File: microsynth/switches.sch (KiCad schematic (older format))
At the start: 35 parts, among them SW12 SW_DPTT_SELECTOR, SW13 SW_DPTT_SELECTOR, SW14 SW_SPDT, SW15 SW_SPDT, SW16 SW_SPDT, SW17 SW_SPDT, SW2 SW_Rotary2x6, SW21 SW_Rotary2x6, SW3 SW_DPTT_SELECTOR, SW4 SW_DPTT_SELECTOR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

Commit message: Footprints 2
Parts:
- C8: footprint (none) -> Capacitor_THT:C_Disc_D5.0mm_W2.5mm_P5.00mm
- SW12, SW13, SW3, SW4, SW6: footprint (none) -> Button_Switch_THT:46313LDRX
- SW2, SW21: footprint (none) -> Rotary_Encoder:rotary-12
- U22: footprint (none) -> Package_DIP:DIP-14_W7.62mm_LongPads
- U7: footprint (none) -> Package_DIP:DIP-8_W7.62mm_LongPads
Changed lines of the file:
@@
 F 0 "SW6" H 2394 3979 50  0000 L CNN
 F 1 "SW_DPTT_SELECTOR" H 2394 3888 50  0000 L CNN
-F 2 "" H 2200 3850 50  0001 C CNN
+F 2 "Button_Switch_THT:46313LDRX" H 2200 3850 50  0001 C CNN
 F 3 "" H 2200 3850 50  0001 C CNN
 	2    2200 3850
@@
 F 0 "SW3" H 7594 1338 50  0000 L CNN
 F 1 "SW_DPTT_SELECTOR" H 7594 1247 50  0000 L CNN
-F 2 "" H 7400 1350 50  0001 C CNN
+F 2 "Button_Switch_THT:46313LDRX" H 7400 1350 50  0001 C CNN
 F 3 "" H 7400 1350 50  0001 C CNN
 	1    7400 1350
@@
 F 0 "SW3" H 7594 1379 50  0000 L CNN
 F 1 "SW_DPTT_SELECTOR" H 7594 1288 50  0000 L CNN
-F 2 "" H 7400 1250 50  0001 C CNN
+F 2 "Button_Switch_THT:46313LDRX" H 7400 1250 50  0001 C CNN
 F 3 "" H 7400 1250 50  0001 C CNN
 	2    7400 1250
@@
 F 0 "SW4" H 9344 1338 50  0000 L CNN
 F 1 "SW_DPTT_SELECTOR" H 9344 1247 50  0000 L CNN
-F 2 "" H 9150 1350 50  0001 C CNN
+F 2 "Button_Switch_THT:46313LDRX" H 9150 1350 50  0001 C CNN
 F 3 "" H 9150 1350 50  0001 C CNN
 	1    9150 1350
@@
 F 0 "SW4" H 9344 1379 50  0000 L CNN
 F 1 "SW_DPTT_SELECTOR" H 9344 1288 50  0000 L CNN
-F 2 "" H 9150 1250 50  0001 C CNN
+F 2 "Button_Switch_THT:46313LDRX" H 9150 1250 50  0001 C CNN
 F 3 "" H 9150 1250 50  0001 C CNN
 	2    9150 1250
@@
 F 0 "U22" H 9650 3581 50  0000 C CNN
 F 1 "4013" H 9650 3490 50  0000 C CNN
-F 2 "" H 9650 3100 50  0001 C CNN
+F 2 "Package_DIP:DIP-14_W7.62mm_LongPads" H 9650 3100 50  0001 C CNN
 F 3 "http://www.onsemi.com/pub/Collateral/MC14013B-D.PDF" H 9650 3100 50  0001 C CNN
 	1    9650 3100
@@
 F 0 "U22" H 8980 4396 50  0000 L CNN
 F 1 "4013" H 8980 4305 50  0000 L CNN
-F 2 "" H 8750 4350 50  0001 C CNN
+F 2 "Package_DIP:DIP-14_W7.62mm_LongPads" H 8750 4350 50  0001 C CNN
 F 3 "http://www.onsemi.com/pub/Collateral/MC14013B-D.PDF" H 8750 4350 50  0001 C CNN
 	3    8750 4350
@@
 F 0 "U22" H 9650 4831 50  0000 C CNN
 F 1 "4013" H 9650 4740 50  0000 C CNN
-F 2 "" H 9650 4350 50  0001 C CNN
+F 2 "Package_DIP:DIP-14_W7.62mm_LongPads" H 9650 4350 50  0001 C CNN
 F 3 "http://www.onsemi.com/pub/Collateral/MC14013B-D.PDF" H 9650 4350 50  0001 C CNN
 	2    9650 4350
@@
 F 0 "SW2" H 1750 7221 50  0000 C CNN
 F 1 "SW_Rotary2x6" H 1750 7130 50  0000 C CNN
-F 2 "" H 1600 6950 50  0001 C CNN
+F 2 "Rotary_Encoder:rotary-12" H 1600 6950 50  0001 C CNN
 F 3 "http://cdn-reichelt.de/documents/datenblatt/C200/DS-Serie%23LOR.pdf" H 1600 6950 50  0001 C CNN
 F 4 "Range" H 1750 7039 50  0000 C CNN "Label"
@@
 F 0 "U7" H 3300 7281 50  0000 C CNN
 F 1 "LM741" H 3300 7190 50  0000 C CNN
-F 2 "" H 3350 6850 50  0001 C CNN
+F 2 "Package_DIP:DIP-8_W7.62mm_LongPads" H 3350 6850 50  0001 C CNN
 F 3 "http://www.ti.com/lit/ds/symlink/lm741.pdf" H 3450 6950 50  0001 C CNN
 	1    3300 6800
@@
 F 0 "C8" V 3052 6500 50  0000 C CNN
 F 1 "10n" V 2961 6500 50  0000 C CNN
-F 2 "" H 2838 6350 50  0001 C CNN
+F 2 "Capacitor_THT:C_Disc_D5.0mm_W2.5mm_P5.00mm" H 2838 6350 50  0001 C CNN
 F 3 "~" H 2800 6500 50  0001 C CNN
 	1    2800 6500
@@
 F 0 "SW6" H 2894 2738 50  0000 L CNN
 F 1 "SW_DPTT_SELECTOR" H 2894 2647 50  0000 L CNN
-F 2 "" H 2700 2750 50  0001 C CNN
+F 2 "Button_Switch_THT:46313LDRX" H 2700 2750 50  0001 C CNN
 F 3 "" H 2700 2750 50  0001 C CNN
 	1    2700 2750
@@
 F 0 "SW21" H 1850 2631 50  0000 C CNN
 F 1 "SW_Rotary2x6" H 1850 2540 50  0000 C CNN
-F 2 "" H 1700 2450 50  0001 C CNN
+F 2 "Rotary_Encoder:rotary-12" H 1700 2450 50  0001 C CNN
 F 3 "http://cdn-reichelt.de/documents/datenblatt/C200/DS-Serie%23LOR.pdf" H 1700 2450 50  0001 C CNN
 	1    1800 1850
@@
 F 0 "SW12" H 5594 4488 50  0000 L CNN
 F 1 "SW_DPTT_SELECTOR" H 5594 4397 50  0000 L CNN
-F 2 "" H 5400 4500 50  0001 C CNN
+F 2 "Button_Switch_THT:46313LDRX" H 5400 4500 50  0001 C CNN
 F 3 "" H 5400 4500 50  0001 C CNN
 	1    5400 4500
@@
 F 0 "SW12" H 5594 4629 50  0000 L CNN
 F 1 "SW_DPTT_SELECTOR" H 5594 4538 50  0000 L CNN
-F 2 "" H 5400 4500 50  0001 C CNN
+F 2 "Button_Switch_THT:46313LDRX" H 5400 4500 50  0001 C CNN
 F 3 "" H 5400 4500 50  0001 C CNN
 	2    5400 4500
@@
 F 0 "SW13" H 7394 4438 50  0000 L CNN
 F 1 "SW_DPTT_SELECTOR" H 7394 4347 50  0000 L CNN
-F 2 "" H 7200 4450 50  0001 C CNN
+F 2 "Button_Switch_THT:46313LDRX" H 7200 4450 50  0001 C CNN
 F 3 "" H 7200 4450 50  0001 C CNN
 	1    7200 4450
@@
 F 0 "SW13" H 7394 4579 50  0000 L CNN
 F 1 "SW_DPTT_SELECTOR" H 7394 4488 50  0000 L CNN
-F 2 "" H 7200 4450 50  0001 C CNN
+F 2 "Button_Switch_THT:46313LDRX" H 7200 4450 50  0001 C CNN
 F 3 "" H 7200 4450 50  0001 C CNN
 	2    7200 4450

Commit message: Hacking together the footprints
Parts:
- RV20: value 10k -> 10kLOG; footprint (none) -> 4ms_Potentiometer:Pot_16mm_NoDet_RV16AF-4A
- RV27: value 4.7k -> 4.7kLOG; footprint (none) -> 4ms_Potentiometer:Pot_16mm_NoDet_RV16AF-4A
- RV28: value 1k -> 1kLIN; footprint (none) -> 4ms_Potentiometer:Pot_16mm_NoDet_RV16AF-4A
- RV4, RV5, RV6, RV7, RV8: footprint (none) -> Potentiometers:Potentiometer_Trimmer_Bourns_PV36W
- SW12, SW13, SW3, SW4, SW6: footprint Button_Switch_THT:46313LDRX -> Buttons_Switches_ThroughHole:DP3T_Toggle; symbol Switch:SW_DPTT_SELECTOR -> microsynth-rescue:SW_DPTT_SELECTOR-Switch
- SW14, SW15, SW16, SW17, SW5: footprint (none) -> 4ms:SPDT_KIT
- SW2, SW21: footprint Rotary_Encoder:rotary-12 -> MyKi_TH_Panel_Controls:SW_Rotary4+12
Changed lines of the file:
@@
 $EndDescr
 $Comp
-L Switch:SW_DPTT_SELECTOR SW6
+L microsynth-rescue:SW_DPTT_SELECTOR-Switch SW6
 U 2 1 5E4ABA98
 P 2200 3850
+AR Path="/5E4ABA98" Ref="SW6"  Part="2"
+AR Path="/5E475532/5E4ABA98" Ref="SW6"  Part="2"
 F 0 "SW6" H 2394 3979 50  0000 L CNN
 F 1 "SW_DPTT_SELECTOR" H 2394 3888 50  0000 L CNN
-F 2 "Button_Switch_THT:46313LDRX" H 2200 3850 50  0001 C CNN
+F 2 "Buttons_Switches_ThroughHole:DP3T_Toggle" H 2200 3850 50  0001 C CNN
 F 3 "" H 2200 3850 50  0001 C CNN
 	2    2200 3850
@@
 $EndComp
 $Comp
-L Switch:SW_DPTT_SELECTOR SW3
+L microsynth-rescue:SW_DPTT_SELECTOR-Switch SW3
 U 1 1 5E4BC6EF
 P 7400 1350
+AR Path="/5E4BC6EF" Ref="SW3"  Part="1"
+AR Path="/5E475532/5E4BC6EF" Ref="SW3"  Part="1"
 F 0 "SW3" H 7594 1338 50  0000 L CNN
 F 1 "SW_DPTT_SELECTOR" H 7594 1247 50  0000 L CNN
-F 2 "Button_Switch_THT:46313LDRX" H 7400 1350 50  0001 C CNN
+F 2 "Buttons_Switches_ThroughHole:DP3T_Toggle" H 7400 1350 50  0001 C CNN
 F 3 "" H 7400 1350 50  0001 C CNN
 	1    7400 1350
@@
 $EndComp
 $Comp
-L Switch:SW_DPTT_SELECTOR SW3
+L microsynth-rescue:SW_DPTT_SELECTOR-Switch SW3
 U 2 1 5E4BCFE7
 P 7400 1250
+AR Path="/5E4BCFE7" Ref="SW3"  Part="2"
+AR Path="/5E475532/5E4BCFE7" Ref="SW3"  Part="2"
 F 0 "SW3" H 7594 1379 50  0000 L CNN
 F 1 "SW_DPTT_SELECTOR" H 7594 1288 50  0000 L CNN
-F 2 "Button_Switch_THT:46313LDRX" H 7400 1250 50  0001 C CNN
+F 2 "Buttons_Switches_ThroughHole:DP3T_Toggle" H 7400 1250 50  0001 C CNN
 F 3 "" H 7400 1250 50  0001 C CNN
 	2    7400 1250
@@
 NoConn ~ 7250 1550
 $Comp
-L Switch:SW_DPTT_SELECTOR SW4
+L microsynth-rescue:SW_DPTT_SELECTOR-Switch SW4
 U 1 1 5E4C21F7
 P 9150 1350
+AR Path="/5E4C21F7" Ref="SW4"  Part="1"
+AR Path="/5E475532/5E4C21F7" Ref="SW4"  Part="1"
 F 0 "SW4" H 9344 1338 50  0000 L CNN
 F 1 "SW_DPTT_SELECTOR" H 9344 1247 50  0000 L CNN
-F 2 "Button_Switch_THT:46313LDRX" H 9150 1350 50  0001 C CNN
+F 2 "Buttons_Switches_ThroughHole:DP3T_Toggle" H 9150 1350 50  0001 C CNN
 F 3 "" H 9150 1350 50  0001 C CNN
 	1    9150 1350
@@
 $EndComp
 $Comp
-L Switch:SW_DPTT_SELECTOR SW4
+L microsynth-rescue:SW_DPTT_SELECTOR-Switch SW4
 U 2 1 5E4C2687
 P 9150 1250
+AR Path="/5E4C2687" Ref="SW4"  Part="2"
+AR Path="/5E475532/5E4C2687" Ref="SW4"  Part="2"
 F 0 "SW4" H 9344 1379 50  0000 L CNN
 F 1 "SW_DPTT_SELECTOR" H 9344 1288 50  0000 L CNN
-F 2 "Button_Switch_THT:46313LDRX" H 9150 1250 50  0001 C CNN
+F 2 "Buttons_Switches_ThroughHole:DP3T_Toggle" H 9150 1250 50  0001 C CNN
 F 3 "" H 9150 1250 50  0001 C CNN
 	2    9150 1250
@@
 F 0 "SW5" V 10604 1112 50  0000 R CNN
 F 1 "SW_SPDT" V 10695 1112 50  0000 R CNN
-F 2 "" H 10650 1300 50  0001 C CNN
+F 2 "4ms:SPDT_KIT" H 10650 1300 50  0001 C CNN
 F 3 "~" H 10650 1300 50  0001 C CNN
 	1    10650 1300
@@
 F 0 "SW2" H 1750 7221 50  0000 C CNN
 F 1 "SW_Rotary2x6" H 1750 7130 50  0000 C CNN
-F 2 "Rotary_Encoder:rotary-12" H 1600 6950 50  0001 C CNN
+F 2 "MyKi_TH_Panel_Controls:SW_Rotary4+12" H 1600 6950 50  0001 C CNN
 F 3 "http://cdn-reichelt.de/documents/datenblatt/C200/DS-Serie%23LOR.pdf" H 1600 6950 50  0001 C CNN
 F 4 "Range" H 1750 7039 50  0000 C CNN "Label"
@@
 F 0 "RV4" V 3735 5750 50  0000 C CNN
 F 1 "10k" V 3644 5750 50  0000 C CNN
-F 2 "" H 3850 5750 50  0001 C CNN
+F 2 "Potentiometers:Potentiometer_Trimmer_Bourns_PV36W" H 3850 5750 50  0001 C CNN
 F 3 "~" H 3850 5750 50  0001 C CNN
 	1    3850 5750
@@
 F 0 "RV5" V 4135 5850 50  0000 C CNN
 F 1 "10k" V 4044 5850 50  0000 C CNN
-F 2 "" H 4250 5850 50  0001 C CNN
+F 2 "Potentiometers:Potentiometer_Trimmer_Bourns_PV36W" H 4250 5850 50  0001 C CNN
 F 3 "~" H 4250 5850 50  0001 C CNN
 	1    4250 5850
@@
 F 0 "RV6" V 4435 6050 50  0000 C CNN
 F 1 "47k" V 4344 6050 50  0000 C CNN
-F 2 "" H 4550 6050 50  0001 C CNN
+F 2 "Potentiometers:Potentiometer_Trimmer_Bourns_PV36W" H 4550 6050 50  0001 C CNN
 F 3 "~" H 4550 6050 50  0001 C CNN
 	1    4550 6050
@@
 F 0 "RV7" V 4735 6150 50  0000 C CNN
 F 1 "47k" V 4644 6150 50  0000 C CNN
-F 2 "" H 4850 6150 50  0001 C CNN
+F 2 "Potentiometers:Potentiometer_Trimmer_Bourns_PV36W" H 4850 6150 50  0001 C CNN
 F 3 "~" H 4850 6150 50  0001 C CNN
 	1    4850 6150
@@
 F 0 "RV8" V 2843 7450 50  0000 C CNN
 F 1 "10k" V 2934 7450 50  0000 C CNN
-F 2 "" H 3050 7450 50  0001 C CNN
+F 2 "Potentiometers:Potentiometer_Trimmer_Bourns_PV36W" H 3050 7450 50  0001 C CNN
 F 3 "~" H 3050 7450 50  0001 C CNN
 	1    3050 7450
@@
 	2200 2250 2400 2250
 $Comp
-L Switch:SW_DPTT_SELECTOR SW6
+L microsynth-rescue:SW_DPTT_SELECTOR-Switch SW6
 U 1 1 5E4A877E
 P 2700 2750
+AR Path="/5E4A877E" Ref="SW6"  Part="1"
+AR Path="/5E475532/5E4A877E" Ref="SW6"  Part="1"
 F 0 "SW6" H 2894 2738 50  0000 L CNN
 F 1 "SW_DPTT_SELECTOR" H 2894 2647 50  0000 L CNN
-F 2 "Button_Switch_THT:46313LDRX" H 2700 2750 50  0001 C CNN
+F 2 "Buttons_Switches_ThroughHole:DP3T_Toggle" H 2700 2750 50  0001 C CNN
 F 3 "" H 2700 2750 50  0001 C CNN
 	1    2700 2750
@@
 F 0 "SW17" H 3600 2635 50  0000 C CNN
 F 1 "SW_SPDT" H 3600 2544 50  0000 C CNN
-F 2 "" H 3600 2350 50  0001 C CNN
+F 2 "4ms:SPDT_KIT" H 3600 2350 50  0001 C CNN
 F 3 "~" H 3600 2350 50  0001 C CNN
 	1    3600 2350
@@
 F 0 "SW16" H 3600 2135 50  0000 C CNN
 F 1 "SW_SPDT" H 3600 2044 50  0000 C CNN
-F 2 "" H 3600 1850 50  0001 C CNN
+F 2 "4ms:SPDT_KIT" H 3600 1850 50  0001 C CNN
 F 3 "~" H 3600 1850 50  0001 C CNN
 	1    3600 1850
@@
 F 0 "SW15" H 3600 1635 50  0000 C CNN
 F 1 "SW_SPDT" H 3600 1544 50  0000 C CNN
-F 2 "" H 3600 1350 50  0001 C CNN
+F 2 "4ms:SPDT_KIT" H 3600 1350 50  0001 C CNN
 F 3 "~" H 3600 1350 50  0001 C CNN
 	1    3600 1350
@@
 F 0 "SW14" H 3600 1135 50  0000 C CNN
 F 1 "SW_SPDT" H 3600 1044 50  0000 C CNN
-F 2 "" H 3600 850 50  0001 C CNN
+F 2 "4ms:SPDT_KIT" H 3600 850 50  0001 C CNN
 F 3 "~" H 3600 850 50  0001 C CNN
 	1    3600 850
@@
 F 0 "SW21" H 1850 2631 50  0000 C CNN
 F 1 "SW_Rotary2x6" H 1850 2540 50  0000 C CNN
-F 2 "Rotary_Encoder:rotary-12" H 1700 2450 50  0001 C CNN
+F 2 "MyKi_TH_Panel_Controls:SW_Rotary4+12" H 1700 2450 50  0001 C CNN
 F 3 "http://cdn-reichelt.de/documents/datenblatt/C200/DS-Serie%23LOR.pdf" H 1700 2450 50  0001 C CNN
 	1    1800 1850
@@
 P 2550 1700
 F 0 "RV20" H 2480 1746 50  0000 R CNN
-F 1 "10k" H 2480 1655 50  0000 R CNN
-F 2 "" H 2550 1700 50  0001 C CNN
+F 1 "10kLOG" H 2480 1655 50  0000 R CNN
+F 2 "4ms_Potentiometer:Pot_16mm_NoDet_RV16AF-4A" H 2550 1700 50  0001 C CNN
 F 3 "~" H 2550 1700 50  0001 C CNN
 	1    2550 1700
@@
 P 4050 4600
 F 0 "RV28" H 3980 4646 50  0000 R CNN
-F 1 "1k" H 3980 4555 50  0000 R CNN
-F 2 "" H 4050 4600 50  0001 C CNN
+F 1 "1kLIN" H 3980 4555 50  0000 R CNN
+F 2 "4ms_Potentiometer:Pot_16mm_NoDet_RV16AF-4A" H 4050 4600 50  0001 C CNN
 F 3 "~" H 4050 4600 50  0001 C CNN
 	1    4050 4600
@@
 P 6400 4750
 F 0 "RV27" H 6330 4796 50  0000 R CNN
-F 1 "4.7k" H 6330 4705 50  0000 R CNN
-F 2 "" H 6400 4750 50  0001 C CNN
+F 1 "4.7kLOG" H 6330 4705 50  0000 R CNN
+F 2 "4ms_Potentiometer:Pot_16mm_NoDet_RV16AF-4A" H 6400 4750 50  0001 C CNN
 F 3 "~" H 6400 4750 50  0001 C CNN
 	1    6400 4750
@@
 	6400 5000 6400 4900
 $Comp
-L Switch:SW_DPTT_SELECTOR SW12
+L microsynth-rescue:SW_DPTT_SELECTOR-Switch SW12
 U 1 1 5EC4EDF0
 P 5400 4500
+AR Path="/5EC4EDF0" Ref="SW12"  Part="1"
+AR Path="/5E475532/5EC4EDF0" Ref="SW12"  Part="1"
 F 0 "SW12" H 5594 4488 50  0000 L CNN
 F 1 "SW_DPTT_SELECTOR" H 5594 4397 50  0000 L CNN
-F 2 "Button_Switch_THT:46313LDRX" H 5400 4500 50  0001 C CNN
+F 2 "Buttons_Switches_ThroughHole:DP3T_Toggle" H 5400 4500 50  0001 C CNN
 F 3 "" H 5400 4500 50  0001 C CNN
 	1    5400 4500
@@
 $EndComp
 $Comp
-L Switch:SW_DPTT_SELECTOR SW12
+L microsynth-rescue:SW_DPTT_SELECTOR-Switch SW12
 U 2 1 5EC508E1
 P 5400 4500
+AR Path="/5EC508E1" Ref="SW12"  Part="2"
+AR Path="/5E475532/5EC508E1" Ref="SW12"  Part="2"
 F 0 "SW12" H 5594 4629 50  0000 L CNN
 F 1 "SW_DPTT_SELECTOR" H 5594 4538 50  0000 L CNN
-F 2 "Button_Switch_THT:46313LDRX" H 5400 4500 50  0001 C CNN
+F 2 "Buttons_Switches_ThroughHole:DP3T_Toggle" H 5400 4500 50  0001 C CNN
 F 3 "" H 5400 4500 50  0001 C CNN
 	2    5400 4500
@@
 	5550 3900 4950 3900
 $Comp
-L Switch:SW_DPTT_SELECTOR SW13
+L microsynth-rescue:SW_DPTT_SELECTOR-Switch SW13
 U 1 1 5EC8F4DB
 P 7200 4450
+AR Path="/5EC8F4DB" Ref="SW13"  Part="1"
+AR Path="/5E475532/5EC8F4DB" Ref="SW13"  Part="1"
 F 0 "SW13" H 7394 4438 50  0000 L CNN
 F 1 "SW_DPTT_SELECTOR" H 7394 4347 50  0000 L CNN
-F 2 "Button_Switch_THT:46313LDRX" H 7200 4450 50  0001 C CNN
+F 2 "Buttons_Switches_ThroughHole:DP3T_Toggle" H 7200 4450 50  0001 C CNN
 F 3 "" H 7200 4450 50  0001 C CNN
 	1    7200 4450
@@
 $EndComp
 $Comp
-L Switch:SW_DPTT_SELECTOR SW13
+L microsynth-rescue:SW_DPTT_SELECTOR-Switch SW13
 U 2 1 5EC90227
 P 7200 4450
+AR Path="/5EC90227" Ref="SW13"  Part="2"
+AR Path="/5E475532/5EC90227" Ref="SW13"  Part="2"
 F 0 "SW13" H 7394 4579 50  0000 L CNN
 F 1 "SW_DPTT_SELECTOR" H 7394 4488 50  0000 L CNN
-F 2 "Button_Switch_THT:46313LDRX" H 7200 4450 50  0001 C CNN
+F 2 "Buttons_Switches_ThroughHole:DP3T_Toggle" H 7200 4450 50  0001 C CNN
 F 3 "" H 7200 4450 50  0001 C CNN
 	2    7200 4450

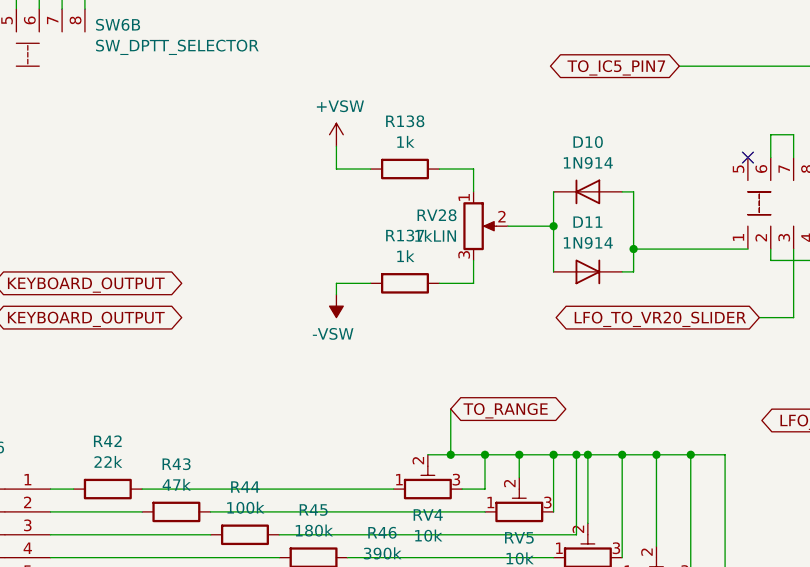
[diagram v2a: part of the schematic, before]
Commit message: Aligned switches and pots
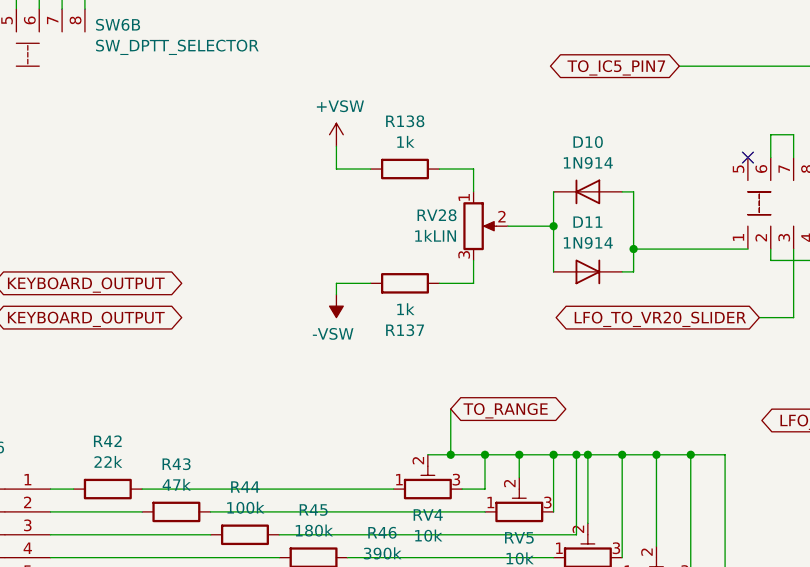
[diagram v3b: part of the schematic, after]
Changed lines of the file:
@@
 F 3 "~" H 3750 4850 50  0001 C CNN
 	1    3750 4850
-	0    1    1    0
+	0    1    -1   0
 $EndComp
 $Comp

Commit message: Laying out pcb
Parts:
- RV20: Label (none) -> VCO2 Level
- RV27: Label (none) -> Thumbwheel
- RV28: Label (none) -> Sweep
- RV4, RV7: footprint Potentiometers:Potentiometer_Trimmer_Bourns_PV36W -> Potentiometers:Potentiometer_WirePads_Small
- SW12: value SW_DPTT_SELECTOR -> SOURCE
- SW13: value SW_DPTT_SELECTOR -> THUMBWEEL
- SW2: value SW_Rotary2x6 -> RANGE
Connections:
- net +VSW: no longer C8.2, R44.1, RV4.2, RV4.3, RV5.2, RV5.3, RV6.2, RV6.3, RV7.2, RV7.3, U7.2 (-)
- net at D10.2 (A), D11.1 (K): now also SW12.5; no longer SW12.1
- net at RV27.1, SW12.2: now also SW12.6, SW12.7
- net at RV27.2, SW13.2: now also SW13.6, SW13.7
- new net TO_RANGE: C8.2, R44.1, RV4.2, RV4.3, RV5.2, RV5.3, RV6.2, RV6.3, RV7.2, RV7.3, U7.2 (-)
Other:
- moved on the sheet: C8, R83, SW6B

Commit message: Laying out pcb ...
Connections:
- net GND: now also RV20.1, RV27.1; no longer RV20.3, RV27.3
- net at SW21.13: now also RV20.3; no longer RV20.1
- net at R138.1: now also RV28.3; no longer RV28.1
- net at R137.1: now also RV28.1; no longer RV28.3
- net at SW12.2, SW12.6, SW12.7: now also RV27.3; no longer RV27.1
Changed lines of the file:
@@
 F 4 "VCO2 Level" H 2450 1550 50  0000 R BNN "Label"
 	1    2550 1700
-	1    0    0    -1
+	1    0    0    1
 $EndComp
 Wire Wire Line
@@
 F 4 "Sweep" H 3950 4450 50  0000 R BNN "Label"
 	1    4050 4600
-	1    0    0    -1
+	1    0    0    1
 $EndComp
 Wire Wire Line
@@
 F 4 "Thumbwheel" H 6300 4600 50  0000 R BNN "Label"
 	1    6400 4750
-	1    0    0    -1
+	1    0    0    1
 $EndComp
 $Comp

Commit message: Layout...
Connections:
- net TO_VCA_C30 renamed LFO_MOD_S17
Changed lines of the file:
@@
 TO_VCF_R99
 Text GLabel 3800 2250 2    50   BiDi ~ 0
-TO_VCA_C30
+LFO_MOD_S17
 Text GLabel 7250 600  2    50   BiDi ~ 0
 TO_VCA_C26

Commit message: Layout...
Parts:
- SW12, SW13, SW3: footprint Buttons_Switches_ThroughHole:DP3T_Toggle -> Buttons_Switches_ThroughHole:L203011MS02Q
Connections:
- net at D10.2 (A), D11.1 (K): now also SW12.1; no longer SW12.5
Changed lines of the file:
@@
 F 0 "SW3" H 7594 1338 50  0000 L CNN
 F 1 "SW_DPTT_SELECTOR" H 7594 1247 50  0000 L CNN
-F 2 "Buttons_Switches_ThroughHole:DP3T_Toggle" H 7400 1350 50  0001 C CNN
+F 2 "Buttons_Switches_ThroughHole:L203011MS02Q" H 7400 1350 50  0001 C CNN
 F 3 "" H 7400 1350 50  0001 C CNN
 	1    7400 1350
@@
 F 0 "SW3" H 7594 1379 50  0000 L CNN
 F 1 "SW_DPTT_SELECTOR" H 7594 1288 50  0000 L CNN
-F 2 "Buttons_Switches_ThroughHole:DP3T_Toggle" H 7400 1250 50  0001 C CNN
+F 2 "Buttons_Switches_ThroughHole:L203011MS02Q" H 7400 1250 50  0001 C CNN
 F 3 "" H 7400 1250 50  0001 C CNN
 	2    7400 1250
@@
 F 0 "SW12" H 5594 4488 50  0000 L CNN
 F 1 "SOURCE" H 5594 4397 50  0000 L CNN
-F 2 "Buttons_Switches_ThroughHole:DP3T_Toggle" H 5400 4500 50  0001 C CNN
+F 2 "Buttons_Switches_ThroughHole:L203011MS02Q" H 5400 4500 50  0001 C CNN
 F 3 "" H 5400 4500 50  0001 C CNN
 	1    5400 4500
@@
 F 0 "SW12" H 5594 4629 50  0000 L CNN
 F 1 "SOURCE" H 5594 4538 50  0000 L CNN
-F 2 "Buttons_Switches_ThroughHole:DP3T_Toggle" H 5400 4500 50  0001 C CNN
+F 2 "Buttons_Switches_ThroughHole:L203011MS02Q" H 5400 4500 50  0001 C CNN
 F 3 "" H 5400 4500 50  0001 C CNN
 	2    5400 4500
 	1    0    0    -1
 $EndComp
-Connection ~ 4750 4700
-Wire Wire Line
-	4750 4700 4750 4800
 Wire Wire Line
 	5350 4700 5350 4750
@@
 F 0 "SW13" H 7394 4438 50  0000 L CNN
 F 1 "THUMBWEEL" H 7394 4347 50  0000 L CNN
-F 2 "Buttons_Switches_ThroughHole:DP3T_Toggle" H 7200 4450 50  0001 C CNN
+F 2 "Buttons_Switches_ThroughHole:L203011MS02Q" H 7200 4450 50  0001 C CNN
 F 3 "" H 7200 4450 50  0001 C CNN
 	1    7200 4450
@@
 F 0 "SW13" H 7394 4579 50  0000 L CNN
 F 1 "THUMBWEEL" H 7394 4488 50  0000 L CNN
-F 2 "Buttons_Switches_ThroughHole:DP3T_Toggle" H 7200 4450 50  0001 C CNN
+F 2 "Buttons_Switches_ThroughHole:L203011MS02Q" H 7200 4450 50  0001 C CNN
 F 3 "" H 7200 4450 50  0001 C CNN
 	2    7200 4450
@@
 	3250 650  3250 850
 Connection ~ 3250 850
-Wire Wire Line
-	4750 4450 4750 4700
 Text GLabel 1200 900  2    50   BiDi ~ 0
 TO_VR20_SLIDER_VCO2_OUTPUT
@@
 Connection ~ 5350 4300
 Wire Wire Line
-	5100 4700 5100 4200
-Wire Wire Line
-	5100 4200 5250 4200
-Wire Wire Line
-	5250 4200 5250 4300
-Wire Wire Line
-	5100 4700 4750 4700
-Wire Wire Line
 	5150 6150 5150 6900
 Wire Wire Line
@@
 Wire Wire Line
 	2950 6300 3650 6300
-NoConn ~ 5250 4700
 Wire Wire Line
 	7150 4250 7150 4650
@@
 TO_KBD_R141
 NoConn ~ 3800 950
+Wire Wire Line
+	4750 4450 4750 4600
+NoConn ~ 5250 4300
+Wire Wire Line
+	5250 4700 5250 4750
+Wire Wire Line
+	5250 4750 5050 4750
+Wire Wire Line
+	5050 4750 5050 4600
+Wire Wire Line
+	5050 4600 4750 4600
+Connection ~ 4750 4600
+Wire Wire Line
+	4750 4600 4750 4800
 $EndSCHEMATC

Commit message: Change switch footprints
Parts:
- SW4, SW6: footprint Buttons_Switches_ThroughHole:DP3T_Toggle -> Buttons_Switches_ThroughHole:L203011MS02Q
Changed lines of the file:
@@
 F 0 "SW6" H 6294 3079 50  0000 L CNN
 F 1 "SW_DPTT_SELECTOR" H 6294 2988 50  0000 L CNN
-F 2 "Buttons_Switches_ThroughHole:DP3T_Toggle" H 6100 2950 50  0001 C CNN
+F 2 "Buttons_Switches_ThroughHole:L203011MS02Q" H 6100 2950 50  0001 C CNN
 F 3 "" H 6100 2950 50  0001 C CNN
 	2    6100 2950
@@
 F 0 "SW4" H 9344 1338 50  0000 L CNN
 F 1 "SW_DPTT_SELECTOR" H 9344 1247 50  0000 L CNN
-F 2 "Buttons_Switches_ThroughHole:DP3T_Toggle" H 9150 1350 50  0001 C CNN
+F 2 "Buttons_Switches_ThroughHole:L203011MS02Q" H 9150 1350 50  0001 C CNN
 F 3 "" H 9150 1350 50  0001 C CNN
 	1    9150 1350
@@
 F 0 "SW4" H 9344 1379 50  0000 L CNN
 F 1 "SW_DPTT_SELECTOR" H 9344 1288 50  0000 L CNN
-F 2 "Buttons_Switches_ThroughHole:DP3T_Toggle" H 9150 1250 50  0001 C CNN
+F 2 "Buttons_Switches_ThroughHole:L203011MS02Q" H 9150 1250 50  0001 C CNN
 F 3 "" H 9150 1250 50  0001 C CNN
 	2    9150 1250
@@
 F 0 "SW6" H 2894 2738 50  0000 L CNN
 F 1 "SW_DPTT_SELECTOR" H 2894 2647 50  0000 L CNN
-F 2 "Buttons_Switches_ThroughHole:DP3T_Toggle" H 2700 2750 50  0001 C CNN
+F 2 "Buttons_Switches_ThroughHole:L203011MS02Q" H 2700 2750 50  0001 C CNN
 F 3 "" H 2700 2750 50  0001 C CNN
 	1    2700 2750
